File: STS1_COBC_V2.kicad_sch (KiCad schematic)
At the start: 13 parts, among them U1 coordinate_system

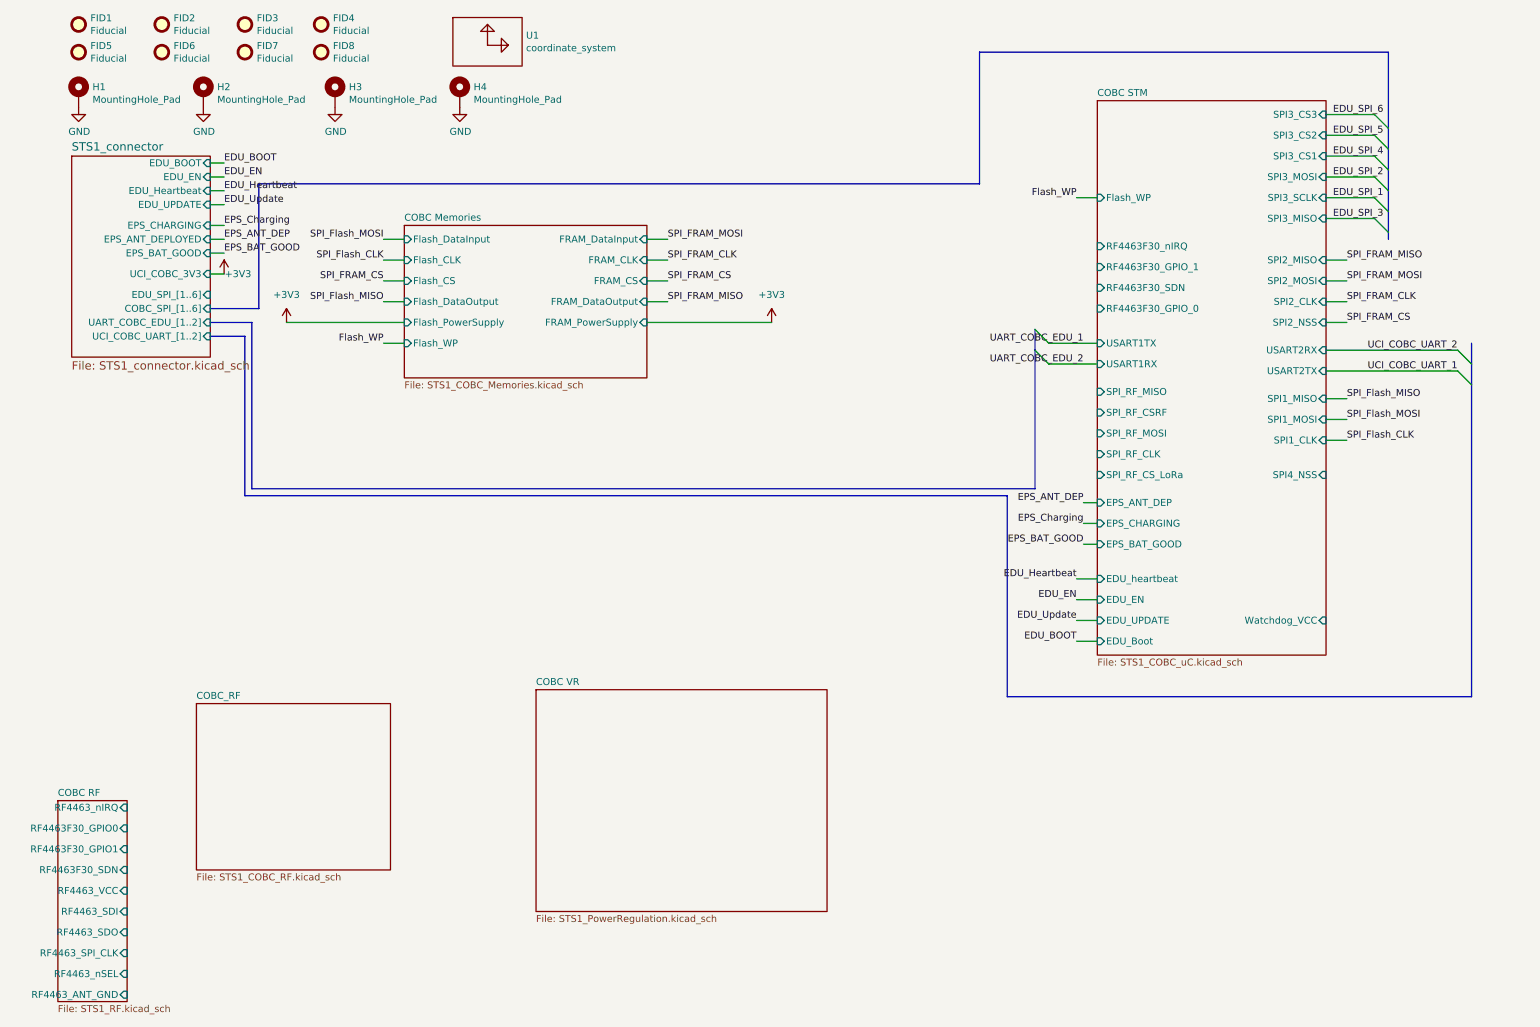
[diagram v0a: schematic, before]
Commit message: more work done
All parts besides RF added
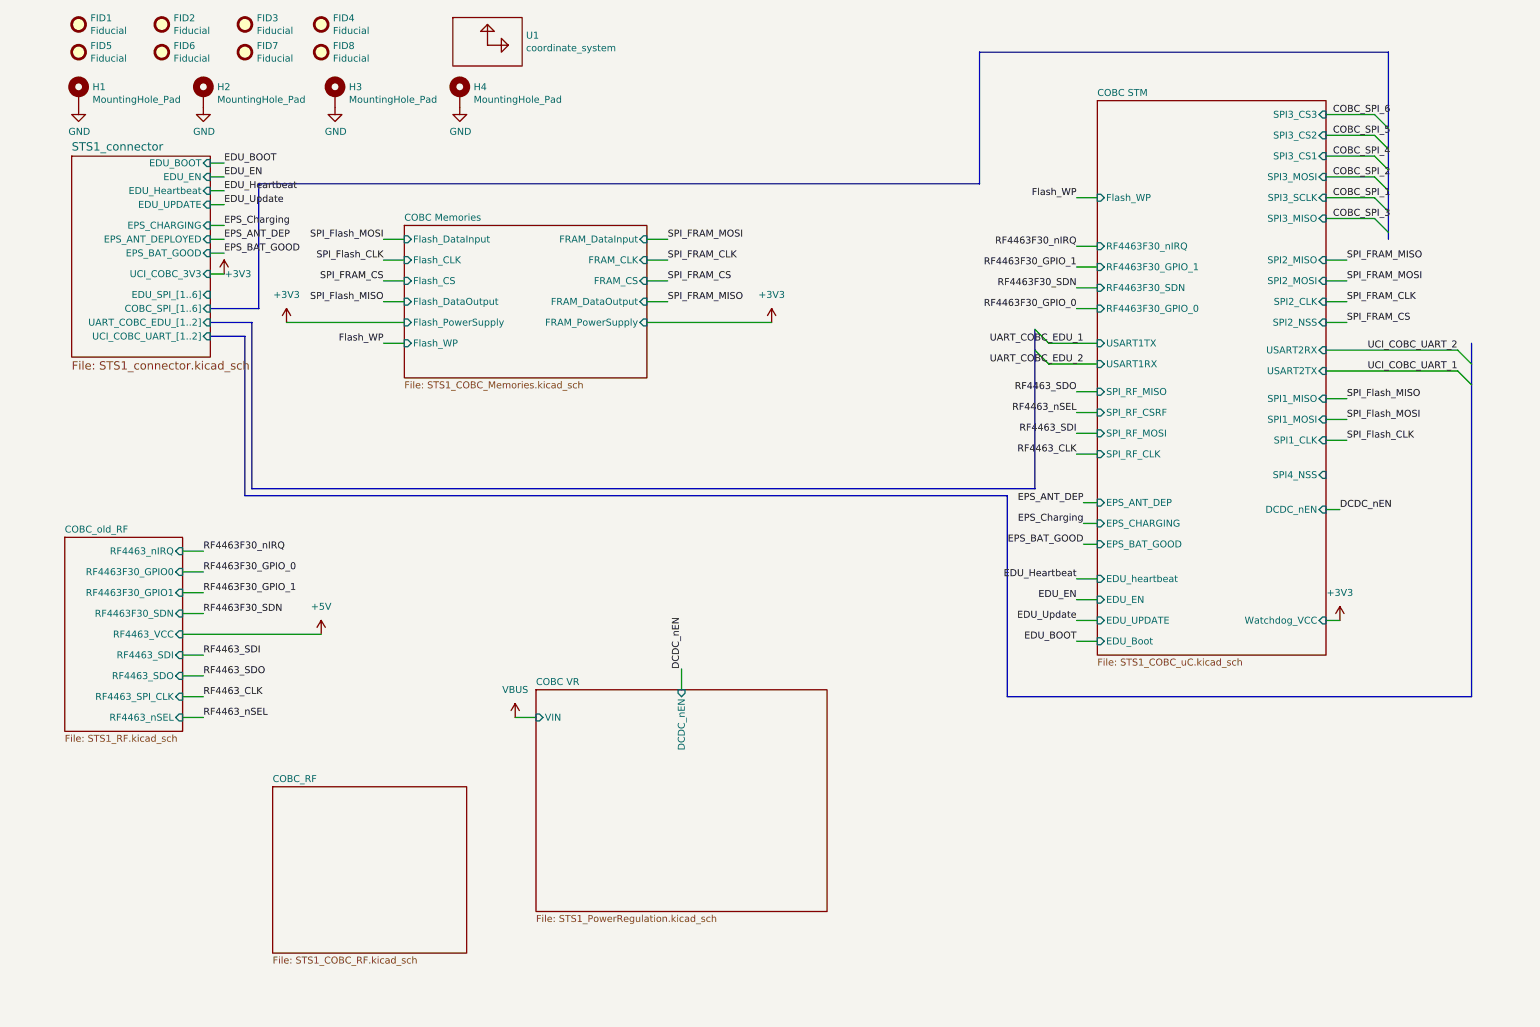
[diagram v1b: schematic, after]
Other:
- removed sheet COBC RF
- added sheet COBC_old_RF (STS1_RF.kicad_sch)
- sheet COBC STM ports: added DCDC_nEN; removed SPI_RF_CS_LoRa
- sheet COBC VR ports: added DCDC_nEN, VIN; removed none

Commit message: add RF part
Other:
- removed sheet COBC_RF
- sheet COBC STM ports: added PA_FAULT, WDT_CLR, ~{WDT_TRIG}; removed none
- sheet COBC_old_RF ports: added PA_FAULT, RF_3V3, RF_5V, Si4463_GPIO0, Si4463_GPIO1, Si4463_SDI, Si4463_SDN, Si4463_SDO, Si4463_SPI_CLK, Si4463_nIRQ, Si4463_nSEL, WDT_CLR, ~{WDT_TRIG}; removed RF4463F30_GPIO0, RF4463F30_GPIO1, RF4463F30_SDN, RF4463_SDI, RF4463_SDO, RF4463_SPI_CLK, RF4463_VCC, RF4463_nIRQ, RF4463_nSEL
- sheet STS1_connector ports: added EPS_BAT_FAULT; removed none

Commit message: ordered version cobc v2
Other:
- sheet COBC STM ports: added EPS_BAT_FAULT; removed SPI4_NSS
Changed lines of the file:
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@@
+    (stroke (width 0) (type default) (color 0 0 0 0))
+  )
+  (wire (pts (xy 45.72 74.93) (xy 45.72 88.9))
     (stroke (width 0) (type default) (color 0 0 0 0))
   )
@@
     (stroke (width 0) (type default) (color 0 0 0 0))
   )
+  (wire (pts (xy 246.38 97.79) (xy 248.92 97.79))
+    (stroke (width 0) (type default) (color 0 0 0 0))
+  )
   (wire (pts (xy 41.91 48.26) (xy 44.45 48.26))
     (stroke (width 0) (type default) (color 0 0 0 0))
@@
     (stroke (width 0) (type default) (color 0 0 0 0))
   )
+  (wire (pts (xy 41.91 88.9) (xy 45.72 88.9))
+    (stroke (width 0) (type default) (color 0 0 0 0))
+  )
   (wire (pts (xy 73.66 62.23) (xy 77.47 62.23))
     (stroke (width 0) (type default) (color 0 0 0 0))
@@
     (stroke (width 0) (type default) (color 0 0 0 0))
   )
+  (wire (pts (xy 41.91 74.93) (xy 45.72 74.93))
+    (stroke (width 0) (type default) (color 0 0 0 0))
+  )
   (wire (pts (xy 246.38 31.75) (xy 255.27 31.75))
     (stroke (width 0) (type default) (color 0 0 0 0))
@@
     (effects (font (size 1.27 1.27)) (justify right bottom))
   )
+  (label "EPS_BAT_FAULT" (at 41.91 88.9 180)
+    (effects (font (size 1.27 1.27)) (justify right bottom))
+  )
   (label "EPS_BAT_GOOD" (at 201.93 110.49 180)
     (effects (font (size 1.27 1.27)) (justify right bottom))
@@
   (label "Si4463_nSEL" (at 54.61 142.24 180)
     (effects (font (size 1.27 1.27)) (justify right bottom))
+  )
+  (label "EPS_BAT_FAULT" (at 248.92 97.79 0)
+    (effects (font (size 1.27 1.27)) (justify left bottom))
   )
   (label "PA_FAULT" (at 53.34 157.48 180)
@@
       (effects (font (size 1.27 1.27)) (justify left))
     )
-    (pin "SPI4_NSS" input (at 246.38 97.79 0)
-      (effects (font (size 1.27 1.27)) (justify right))
-    )
     (pin "RF4463F30_SDN" input (at 204.47 63.5 180)
       (effects (font (size 1.27 1.27)) (justify left))
@@
     )
     (pin "PA_FAULT" input (at 246.38 115.57 0)
+      (effects (font (size 1.27 1.27)) (justify right))
+    )
+    (pin "EPS_BAT_FAULT" input (at 246.38 97.79 0)
       (effects (font (size 1.27 1.27)) (justify right))
     )
@@
       (reference "J17") (unit 1) (value "Conn_01x03_Male") (footprint "STS1library:PinHeader_1x03_P2.54mm_Vertical_umdieEcke")
     )
-    (path "/be3cc363-80eb-4df5-9a1b-912085b5cf84/00000000-0000-0000-0000-00006198ba28"
-      (reference "J18") (unit 1) (value "Conn_01x01_Male") (footprint "Connector_PinHeader_2.54mm:PinHeader_1x01_P2.54mm_Vertical")
-    )
     (path "/a8678e8a-595e-4c52-9d87-4220609965c5/80af458f-c7a5-433b-9df7-795777bcc769"
       (reference "L1") (unit 1) (value "15n") (footprint "Inductor_SMD:L_0402_1005Metric")
@@
       (reference "TP17") (unit 1) (value "TestPoint") (footprint "STS1library:STS1_Testpoint")
     )
-    (path "/be3cc363-80eb-4df5-9a1b-912085b5cf84/f740de66-7842-48d1-8854-c13cd53c0ed3"
-      (reference "TP18") (unit 1) (value "TestPoint") (footprint "STS1library:STS1_Testpoint")
-    )
-    (path "/be3cc363-80eb-4df5-9a1b-912085b5cf84/e6a5633f-c6ca-43a7-bac0-3d0810684409"
-      (reference "TP19") (unit 1) (value "TestPoint") (footprint "STS1library:STS1_Testpoint")
-    )
-    (path "/be3cc363-80eb-4df5-9a1b-912085b5cf84/f0e16474-b13c-47ba-bf3e-2283d8e78b8f"
-      (reference "TP20") (unit 1) (value "TestPoint") (footprint "STS1library:STS1_Testpoint")
-    )
     (path "/a8678e8a-595e-4c52-9d87-4220609965c5/5020136b-5eea-4a2f-9bc4-470d670f3f42/6f0f2ebc-d1a8-4058-9e41-80284bd55907"

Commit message: Remove old submodules
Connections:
- no-connect marks 0 -> 4

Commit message: V2.5
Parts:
- added TP14: TestPoint, STS1library:STS1_Testpoint, symbol Connector:TestPoint
- U1: footprint STS:Coordinates -> STS_connector:Coordinates; symbol STS1_template-rescue:coordinate_system-STS-con -> STS-connector:coordinate_system
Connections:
- net SPI_FRAM_CS: now also TP14.1
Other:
- sheet COBC STM ports: added SPI3_CS4; removed none
